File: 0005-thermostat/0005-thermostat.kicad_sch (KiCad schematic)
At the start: 41 parts, among them J1 EXT_NTC, J2 OUT, J3 PWR, J4 EXT_LED, J5 EXT_P1, J6 EXT_P2, P1 22k, P2 22k, T1 BC847B, T2 BC847B, T3 BC847B

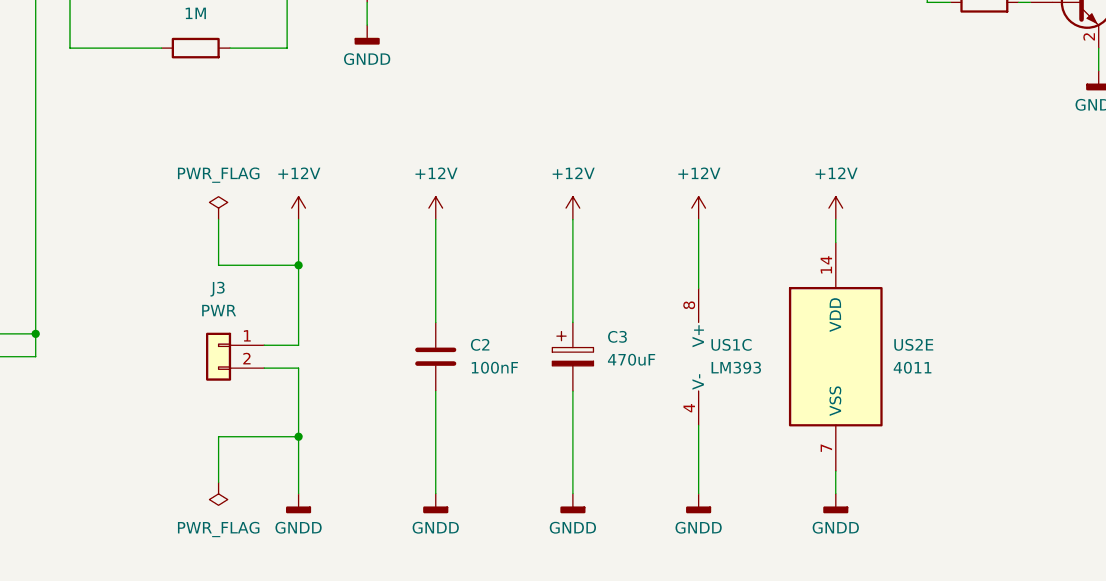
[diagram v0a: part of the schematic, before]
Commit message: PCB enhancement (#6)
* PCB enhancement

* Redesign power plug

* Small PCB changes

* Redesign another sections

* Re-design comparator section, shrink the board

* Redesigned PCB shape

* Replace SOIC to TSSOP ICs footprints
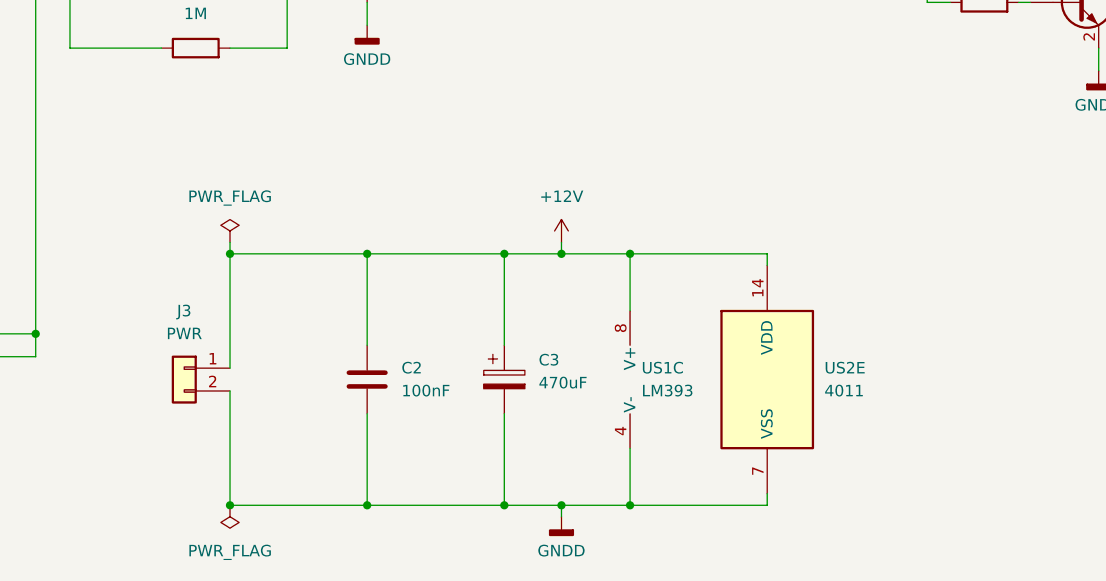
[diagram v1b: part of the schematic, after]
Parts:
- US1: footprint Package_DFN_QFN:DFN-8-1EP_2x2mm_P0.5mm_EP0.8x1.6mm -> Package_SO:TSSOP-8_4.4x3mm_P0.65mm
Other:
- moved on the sheet: C2, C3, J3, US1C, US2E
